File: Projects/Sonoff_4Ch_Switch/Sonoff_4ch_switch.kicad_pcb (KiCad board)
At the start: 2 copper layers, 99.8 x 99.1 mm, 65 parts, among them J1 Barrel_Jack_Switch, J2 Live, J3 Neutrals, J4 Earths, J5 Conn_01x03_Male, K1 G5LE-1, K2 G5LE-1, K3 G5LE-1, K4 G5LE-1, Q1 2N7002, Q2 2N7002, Q3 2N7002, Q4 2N7002, Q5 2N7002, Q6 2N7002, Q7 2N7002, Q8 2N7002, U1 AP1117-15, U2 WeMos_mini

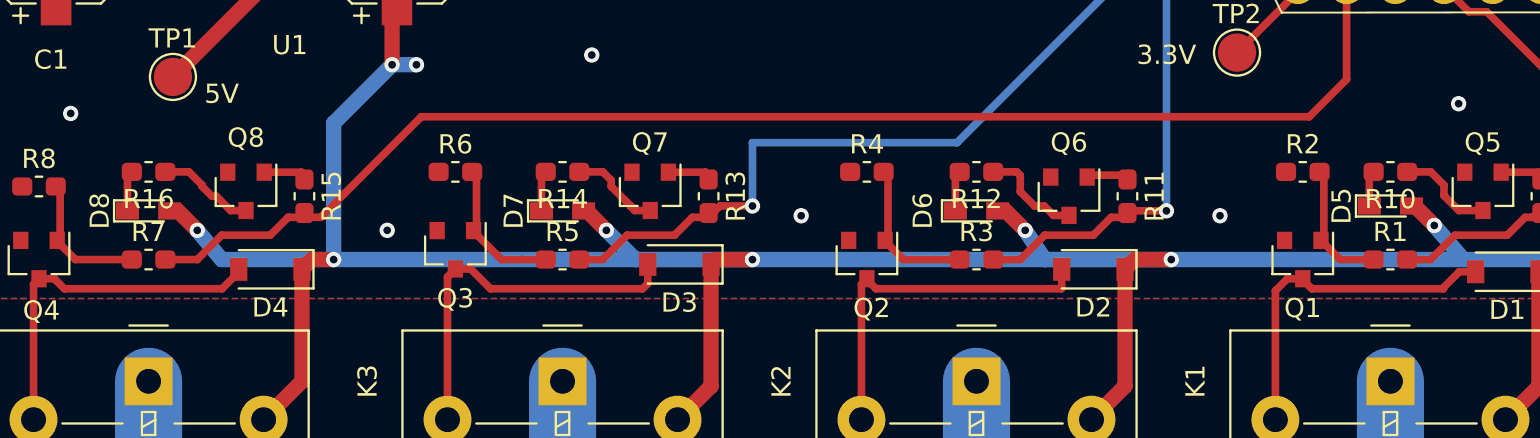
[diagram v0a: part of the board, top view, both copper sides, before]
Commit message: On to rev A2 of the 4 ch switch....
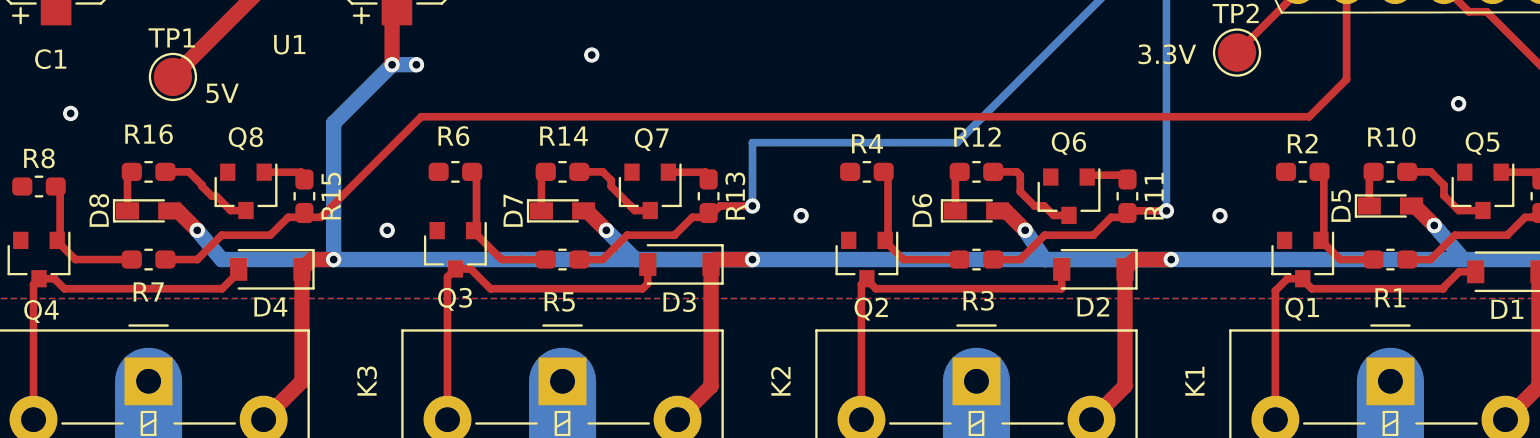
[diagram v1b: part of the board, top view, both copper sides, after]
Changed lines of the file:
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@@
     (47 F.CrtYd user)
     (48 B.Fab user)
-    (49 F.Fab user)
+    (49 F.Fab user hide)
   )
   (setup
@@
     (tags "resistor handsolder")
     (attr smd)
-    (fp_text reference R14 (at 0 -1.43 180) (layer F.SilkS)
+    (fp_text reference R14 (at -0.0508 1.8288 180) (layer F.SilkS)
       (effects (font (size 1 1) (thickness 0.15)))
     )
@@
     (tags "resistor handsolder")
     (attr smd)
-    (fp_text reference R7 (at 0 -1.43) (layer F.SilkS)
+    (fp_text reference R7 (at 0 1.7272) (layer F.SilkS)
       (effects (font (size 1 1) (thickness 0.15)))
     )
@@
     (tags "resistor handsolder")
     (attr smd)
-    (fp_text reference R5 (at 0 -1.43) (layer F.SilkS)
+    (fp_text reference R5 (at -0.1524 2.2352) (layer F.SilkS)
       (effects (font (size 1 1) (thickness 0.15)))
     )
@@
     (tags "resistor handsolder")
     (attr smd)
-    (fp_text reference R6 (at 0 -1.43) (layer F.SilkS)
+    (fp_text reference R6 (at -0.1016 -1.8288) (layer F.SilkS)
       (effects (font (size 1 1) (thickness 0.15)))
     )
@@
     (tags "resistor handsolder")
     (attr smd)
-    (fp_text reference R16 (at 0 -1.43 180) (layer F.SilkS)
+    (fp_text reference R16 (at 0 1.9304 180) (layer F.SilkS)
       (effects (font (size 1 1) (thickness 0.15)))
     )
@@
     (tags "resistor handsolder")
     (attr smd)
-    (fp_text reference R1 (at 0 -1.43) (layer F.SilkS)
+    (fp_text reference R1 (at 0 2.032) (layer F.SilkS)
       (effects (font (size 1 1) (thickness 0.15)))
     )
@@
     (tags "resistor handsolder")
     (attr smd)
-    (fp_text reference R10 (at 0 -1.43 180) (layer F.SilkS)
+    (fp_text reference R10 (at -0.0508 1.778 180) (layer F.SilkS)
       (effects (font (size 1 1) (thickness 0.15)))
     )
@@
     (tags "resistor handsolder")
     (attr smd)
-    (fp_text reference R12 (at 0 -1.43 180) (layer F.SilkS)
+    (fp_text reference R12 (at -0.0508 1.778 180) (layer F.SilkS)
       (effects (font (size 1 1) (thickness 0.15)))
     )
@@
     (tags "resistor handsolder")
     (attr smd)
-    (fp_text reference R3 (at 0 -1.43) (layer F.SilkS)
+    (fp_text reference R3 (at 0.1016 2.1844) (layer F.SilkS)
       (effects (font (size 1 1) (thickness 0.15)))
     )
@@
     (tags SOT-23)
     (attr smd)
-    (fp_text reference Q7 (at -2.54 0) (layer F.SilkS)
-      (effects (font (size 1 1) (thickness 0.15)))
-    )
+    (fp_text reference Q7 (at -2.7432 -0.1016) (layer F.SilkS)
+      (effects (font (size 1 1) (thickness 0.15)))
+    )
